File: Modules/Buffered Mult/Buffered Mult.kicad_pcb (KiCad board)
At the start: 2 copper layers, 50 x 200 mm, 20 parts

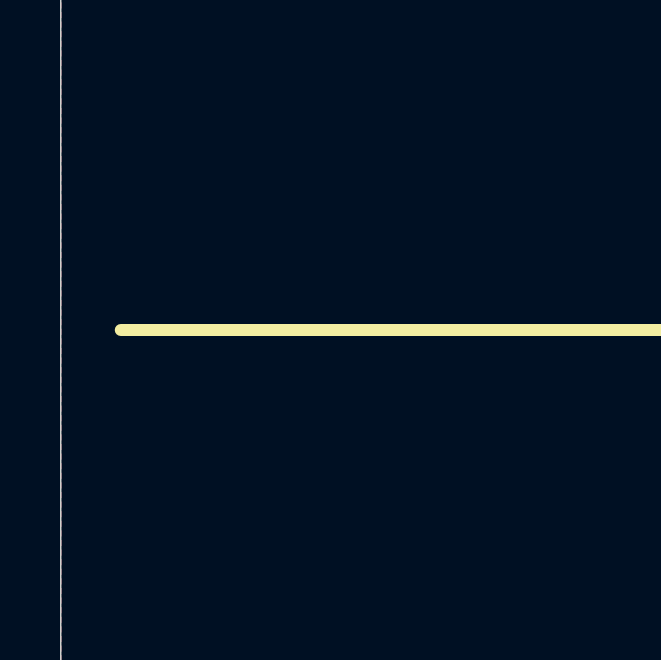
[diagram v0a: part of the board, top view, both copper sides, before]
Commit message: Added 0V solder pad and pin to panel and PCB
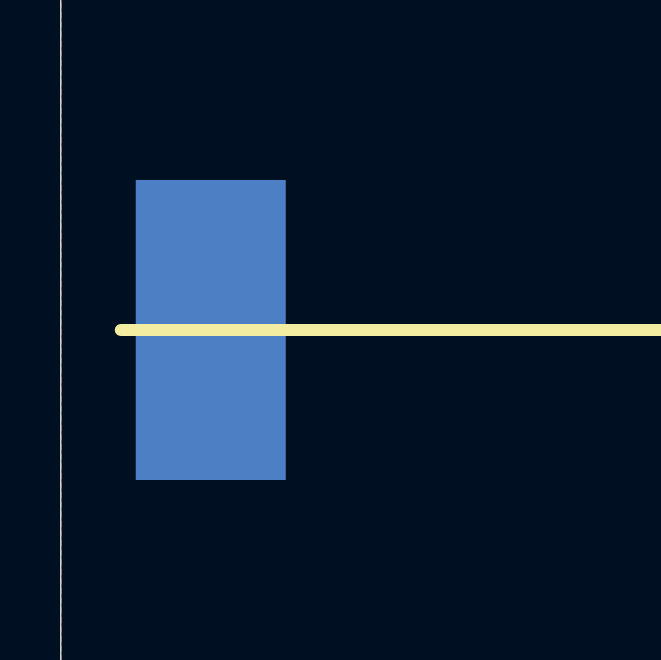
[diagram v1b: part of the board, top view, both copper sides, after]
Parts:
- added J1: 0V, Connector_Wire:SolderWirePad_1x01_SMD_5x10mm, B.Cu at (80.0, 130.0)
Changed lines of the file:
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@@
+		)
+	)
+	(footprint "Connector_Wire:SolderWirePad_1x01_SMD_5x10mm"
+		(layer "B.Cu")
+		(at 80 130 180)
+		(descr "Wire Pad, Square, SMD Pad,  5mm x 10mm,")
+		(tags "MesurementPoint Square SMDPad 5mmx10mm ")
+		(property "Reference" "J1"
+			(at 0 3.81 0)
+			(layer "B.SilkS")
+			(hide yes)
+			(effects
+				(font
+					(size 1 1)
+					(thickness 0.15)
+				)
+				(justify mirror)
+			)
+		)
+		(property "Value" "0V"
+			(at 0 -6.35 0)
+			(layer "B.SilkS")
+			(effects
+				(font
+					(size 1 1)
+					(thickness 0.15)
+				)
+				(justify mirror)
+			)
+		)
+		(property "Footprint" "Connector_Wire:SolderWirePad_1x01_SMD_5x10mm"
+			(at 0 0 0)
+			(unlocked yes)
+			(layer "B.Fab")
+			(hide yes)
+			(effects
+				(font
+					(size 1.27 1.27)
+					(thickness 0.15)
+				)
+				(justify mirror)
+			)
+		)
+		(property "Datasheet" ""
+			(at 0 0 0)
+			(unlocked yes)
+			(layer "B.Fab")
+			(hide yes)
+			(effects
+				(font
+					(size 1.27 1.27)
+					(thickness 0.15)
+				)
+				(justify mirror)
+			)
+		)
+		(property "Description" "Generic connector, single row, 01x01, script generated (kicad-library-utils/schlib/autogen/connector/)"
+			(at 0 0 0)
+			(unlocked yes)
+			(layer "B.Fab")
+			(hide yes)
+			(effects
+				(font
+					(size 1.27 1.27)
+					(thickness 0.15)
+				)
+				(justify mirror)
+			)
+		)
+		(property ki_fp_filters "Connector*:*_1x??_*")
+		(sheetname "Root")
+		(sheetfile "Buffered Mult.kicad_sch")
+		(attr smd exclude_from_pos_files)
+		(fp_line
+			(start 2.75 5.25)
+			(end 2.75 -5.25)
+			(stroke
+				(width 0.05)
+				(type solid)
+			)
+			(layer "B.CrtYd")
+		)
+		(fp_line
+			(start 2.75 -5.25)
+			(end -2.75 -5.25)
+			(stroke
+				(width 0.05)
+				(type solid)
+			)
+			(layer "B.CrtYd")
+		)
+		(fp_line
+			(start -2.75 5.25)
+			(end 2.75 5.25)
+			(stroke
+				(width 0.05)
+				(type solid)
+			)
+			(layer "B.CrtYd")
+		)
+		(fp_line
+			(start -2.75 -5.25)
+			(end -2.75 5.25)
+			(stroke
+				(width 0.05)
+				(type solid)
+			)
+			(layer "B.CrtYd")
+		)
+		(fp_text user "${REFERENCE}"
+			(at 0 0 0)
+			(layer "B.Fab")
+			(effects
+				(font
+					(size 1 1)
+					(thickness 0.15)
+				)
+				(justify mirror)
+			)
+		)
+		(pad "1" smd rect
+			(at 0 0 180)
+			(size 5 10)
+			(layers "B.Cu" "B.Paste" "B.Mask")
+			(net 1 "GND")
+			(pinfunction "Pin_1")
+			(pintype "passive")
 		)
 	)

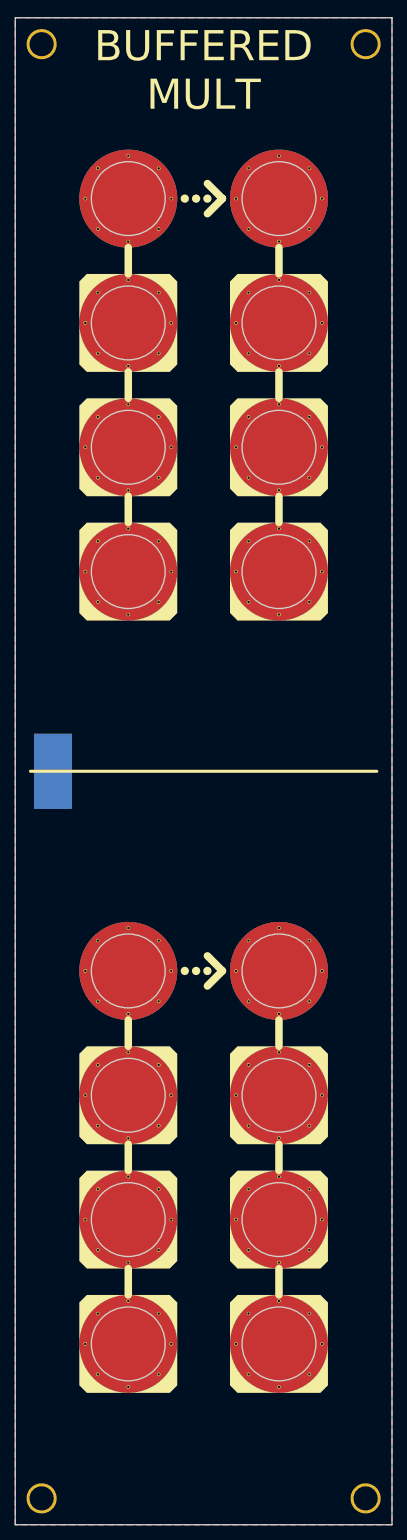
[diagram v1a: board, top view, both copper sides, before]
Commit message: Updated fps to 12mm diameter
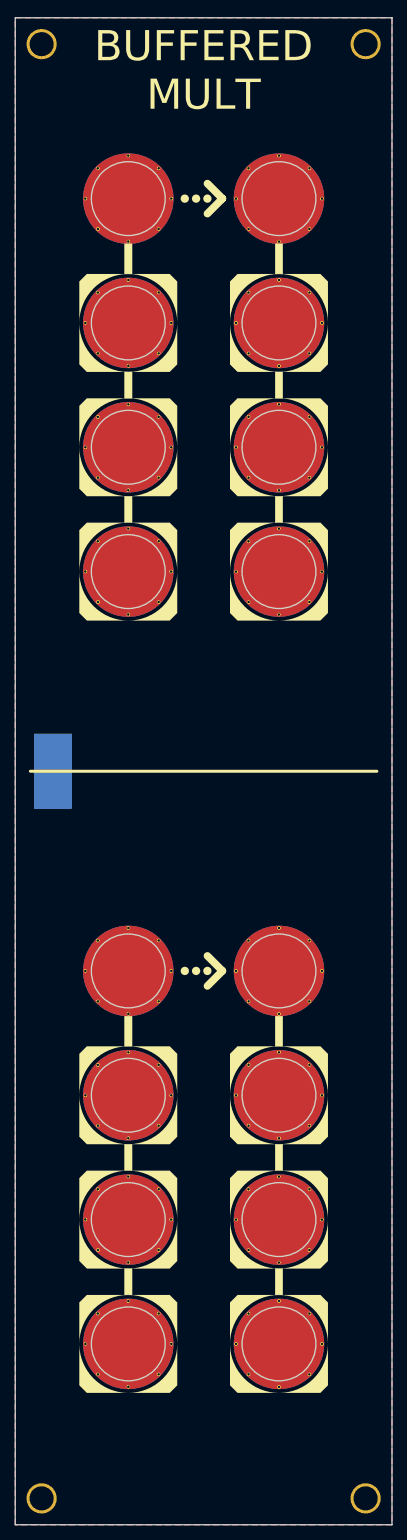
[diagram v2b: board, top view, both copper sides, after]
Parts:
- H1, H2, H3, H4: footprint SynthStuff:MountingHole_3.2mm_M3_Pad4mm -> SynthStuff:MountingHole_Rails
- H10, H11, H12, H15, H16, H17, H18, H19, H20, H7, H8, H9: footprint SynthStuff:Jack_6.35mm_Cutout_Output_v5 -> SynthStuff:Jack_6.35mm_Cutout_Output_v6
- H13, H14, H5, H6: footprint SynthStuff:Jack_6.35mm_Cutout_v2 -> SynthStuff:Jack_6.35mm_Cutout_v3

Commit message: Added space for fab serial number
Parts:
- J1: value 0V -> GND
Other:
- board text added: "JLCJLCJLCJLC"
- board text added: "Mk1 - June 2024"
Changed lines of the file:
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@@
 			)
 		)
-		(property "Value" "0V"
-			(at 0 -6.35 0)
+		(property "Value" "GND"
+			(at 0 -6.75 0)
 			(layer "B.SilkS")
 			(effects
 				(font
-					(size 1 1)
-					(thickness 0.15)
+					(size 1.5 1.5)
+					(thickness 0.3)
+					(bold yes)
 				)
 				(justify mirror)
@@
 		(layer "User.9")
 	)
+	(gr_text "JLCJLCJLCJLC"
+		(at 100 226.5 0)
+		(layer "B.SilkS")
+		(effects
+			(font
+				(size 1.5 1.5)
+				(thickness 0.3)
+				(bold yes)
+			)
+			(justify mirror)
+		)
+	)
+	(gr_text "Mk1 - June 2024"
+		(at 100 223 0)
+		(layer "B.SilkS")
+		(effects
+			(font
+				(size 1.5 1.5)
+				(thickness 0.3)
+				(bold yes)
+			)
+			(justify mirror)
+		)
+	)
 	(gr_text "BUFFERED\nMULT"
